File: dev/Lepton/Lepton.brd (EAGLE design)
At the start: 57.1 x 25.4 mm, 64 parts, among them J1 M12, J2 M12, Q2 CM415, U1 CC3000, U2 STM32F100R4T6B, U3 STM32-JTAG-FFC, U4 SILICONLABS-HUMIDITY-SI7005, U5 FREESCALE-PRESSURE-MPL3115A2, U6 MMA8653FC, X1 USBPCB

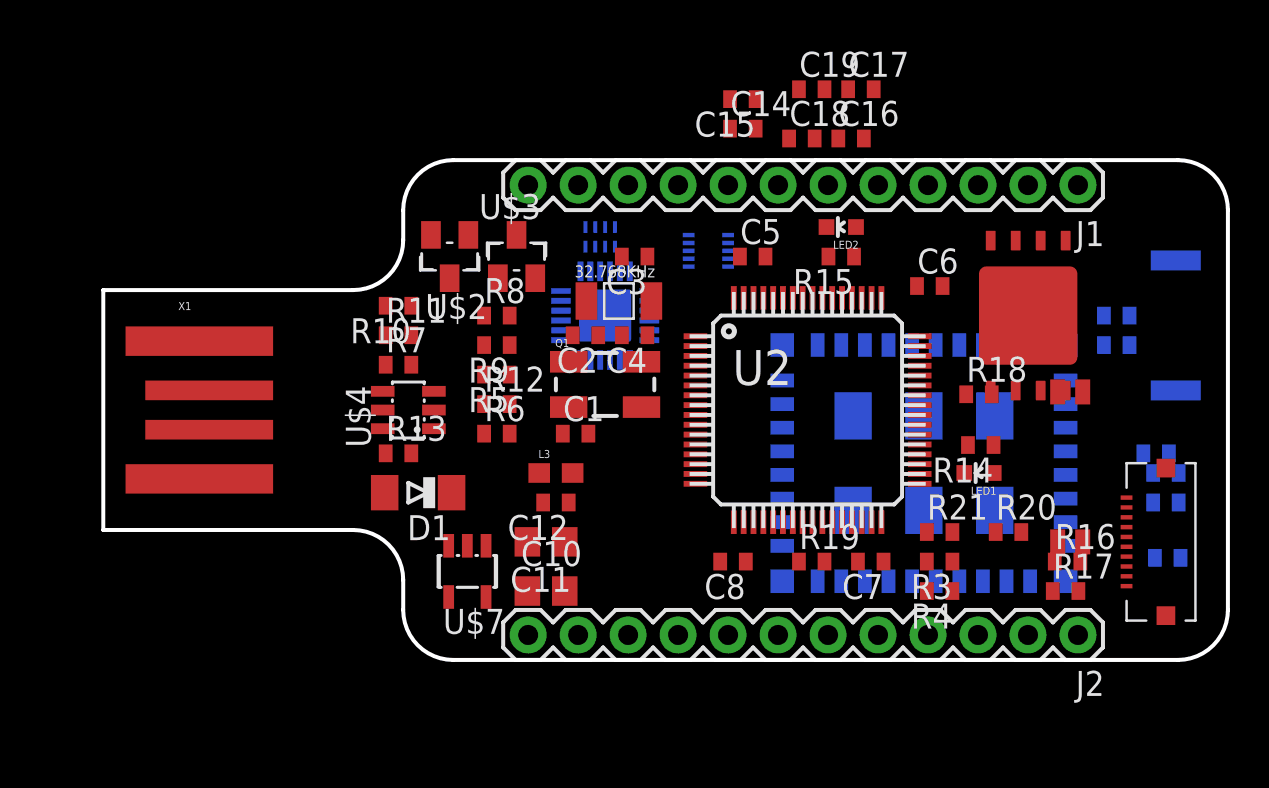
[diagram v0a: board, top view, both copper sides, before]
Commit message: Updated board with smaller components, micro USB, and mounting holes
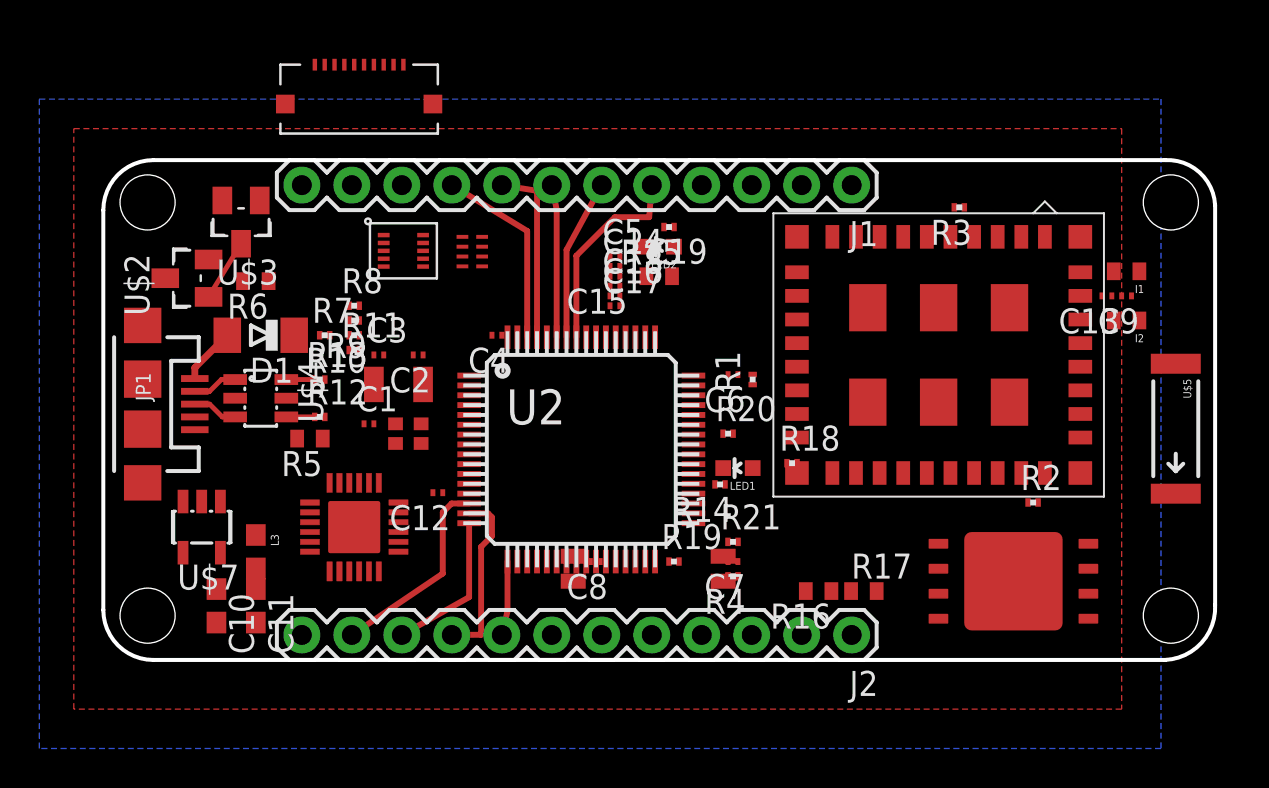
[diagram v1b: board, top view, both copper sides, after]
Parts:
- removed Q1: (no value), Pygmy:CRYSTAL-SMD-5X3
- removed Q2: CM415, Pygmy:CM415
- added JP1: USB-MICROB, SparkFun-Connectors:USB-MICROB
- added X2: CRYSTAL-KYOCERA-ST3215SB, Pygmy:CRYSTAL-KYOCERA-ST3215SB
- C1, C12, C13, C14, C15, C16, C17, C18, C2, C3, C4, C5, C6, C7, C8, C9: device rcl:C0402 -> rcl:C0201
- C10, C11: device rcl:C0805 -> rcl:C0603
- R1, R10, R11, R12, R13, R14, R15, R18, R19, R2, R3, R4, R7, R8, R9: device rcl:R0402 -> rcl:R0201
- R20, R21: value (none) -> 47K; device rcl:R0402 -> rcl:R0201
- X1: value USBPCB -> CRYSTAL-ABRACON-ABM11; device Pygmy:USB-A-PCB -> Pygmy:ABM11
- moved U3 45.9 mm to (13.0, 30.2), turned to 0 degrees
- moved R1 18.6 mm to (33.0, 14.2), flipped to the top, turned to 90 degrees
- moved R3 18.0 mm to (43.5, 23.0)
- moved U1 17.5 mm to (35.2, 21.5), flipped to the top, turned to 270 degrees
- moved U6 17.5 mm to (14.2, 21.6), flipped to the top
- moved S1 17.1 mm to (31.5, 4.00), turned to 90 degrees
- moved C10 16.8 mm to (5.75, 2.75), turned to 270 degrees
- moved U4 16.7 mm to (12.8, 6.75), flipped to the top
- moved C17 16.7 mm to (26.0, 18.0)
- moved L3 15.8 mm to (7.75, 5.50), turned to 270 degrees
- moved C11 15.1 mm to (7.75, 2.75), turned to 270 degrees
- moved R20 15.1 mm to (31.8, 11.5)
- moved R6 14.5 mm to (7.75, 19.2), turned to 180 degrees
- moved C16 14.4 mm to (26.0, 18.5)
- moved U$3 14.1 mm to (7.00, 22.2), turned to 180 degrees
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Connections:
- net EXT0: now also U2.17; no longer U2.14
- net EXT3: now also U2.14; no longer U2.17
- net GND: now also JP1.GND, JP1.MT1, JP1.MT2, X1.P2, X1.P4; no longer X1.GND
- net N$1: now also JP1.D+; no longer X1.USB_P
- net N$2: now also JP1.D-; no longer X1.USB_M
- net N$9: now also JP1.VBUS; no longer X1.5V
- net OSC32_IN: now also X2.P2; no longer Q2.P$2
- net OSC32_OUT: now also X2.P1; no longer Q2.P$1
- net OSC_IN: now also X1.P3; no longer Q1.3
- net OSC_OUT: now also X1.P1; no longer Q1.1
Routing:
- net EXT8: track 0.00 -> 10.3 mm
- net EXT3: track 0.00 -> 10.2 mm
- net EXT12: track 0.00 -> 9.88 mm
- net EXT11: track 0.00 -> 9.25 mm
- net EXT1: track 0.00 -> 8.93 mm
- net EXT9: track 0.00 -> 8.19 mm
- net EXT10: track 0.00 -> 7.75 mm
- net EXT2: track 0.00 -> 7.68 mm
- net EXT0: track 0.00 -> 3.76 mm
- net N$16: track 0.00 -> 3.16 mm
- net N$9: track 0.00 -> 2.88 mm
- net N$1: track 0.00 -> 2.32 mm
- net N$2: track 0.00 -> 2.30 mm
- net N$19: track 0.00 -> 1.44 mm
- net N$14: track 0.00 -> 1.44 mm
- added copper zone on layer 1, net GND
- added copper zone on layer 16, net GND
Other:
- board size 57.1 x 25.4 mm -> 56.5 x 25.4 mm
